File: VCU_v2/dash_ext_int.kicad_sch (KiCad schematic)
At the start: 55 parts, among them Q3 SP8K80TB1, Q4 SP8K80TB1, Q5 SP8K80TB1

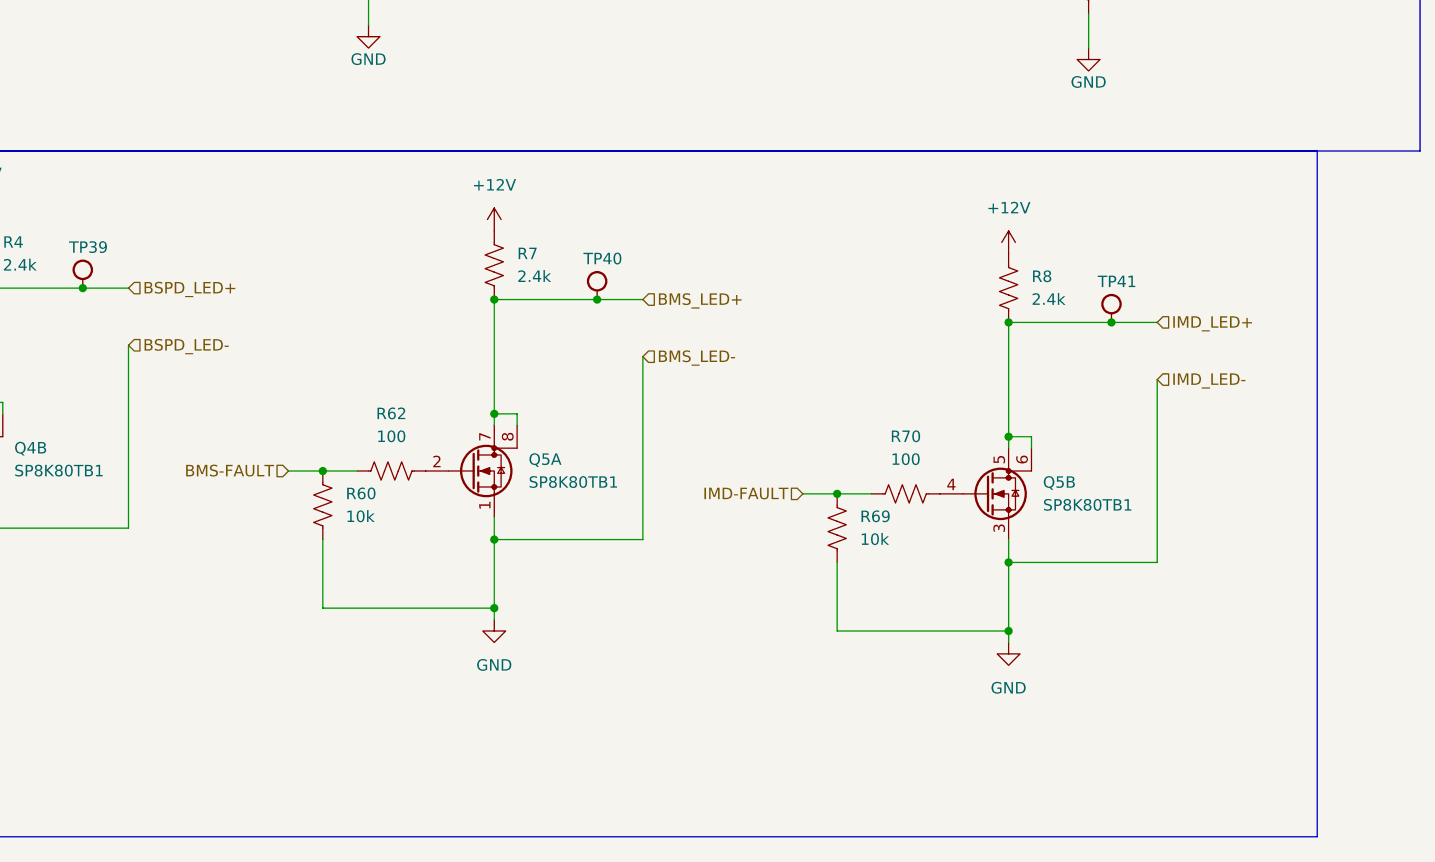
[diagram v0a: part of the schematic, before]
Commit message: reworked shutdown led logi c
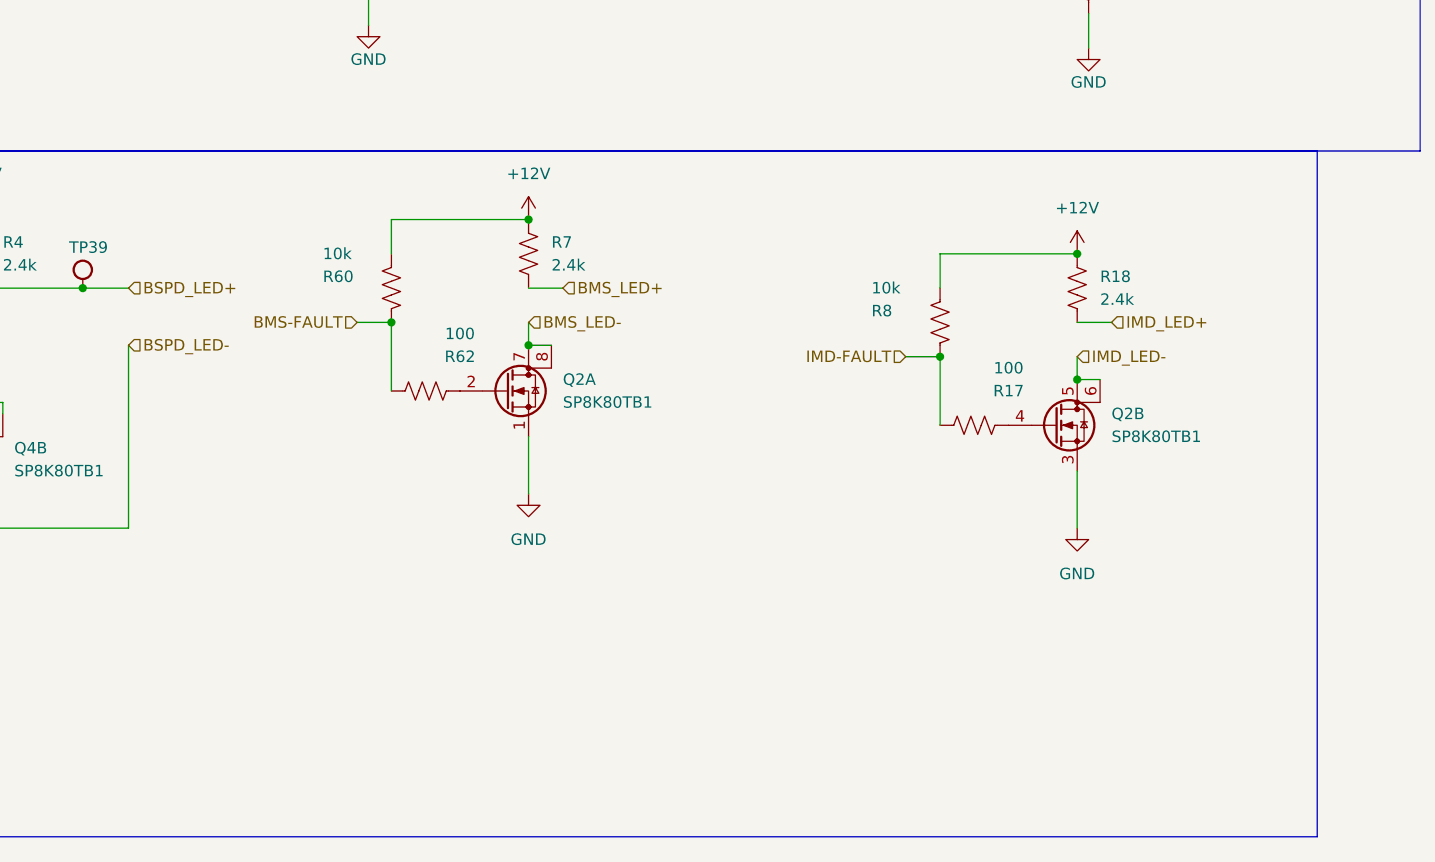
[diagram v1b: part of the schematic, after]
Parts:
- removed Q5: SP8K80TB1, Package_SO:SOP-8_3.76x4.96mm_P1.27mm, symbol Transistor_FET:Q_Dual_NMOS_S1G1S2G2D2D2D1D1
- removed R69: 10k, Resistor_SMD:R_0603_1608Metric_Pad0.98x0.95mm_HandSolder, symbol BFR Resistors:RMCF0603FT10K0
- removed R70: 100, Resistor_SMD:R_0603_1608Metric_Pad0.98x0.95mm_HandSolder, symbol BFR Resistors:RMCF0603FT100R
- removed R8: 2.4k, Resistor_SMD:R_0603_1608Metric_Pad0.98x0.95mm_HandSolder, symbol BFR Resistors:RMCF0603FT2K40
- removed TP40, TP41: RH-5015, TestPoint:TestPoint_Keystone_5015_Micro_Mini, symbol .Test-Point:RH-5015
- added Q2: SP8K80TB1, Package_SO:SOP-8_3.76x4.96mm_P1.27mm, symbol Transistor_FET:Q_Dual_NMOS_S1G1S2G2D2D2D1D1
- added R17: 100, Resistor_SMD:R_0603_1608Metric_Pad0.98x0.95mm_HandSolder, symbol BFR Resistors:RMCF0603FT100R
- added R18: 2.4k, Resistor_SMD:R_0603_1608Metric_Pad0.98x0.95mm_HandSolder, symbol BFR Resistors:RMCF0603FT2K40
- added R8: 10k, Resistor_SMD:R_0603_1608Metric_Pad0.98x0.95mm_HandSolder, symbol BFR Resistors:RMCF0603FT10K0
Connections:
- net +12V: now also R60.1, R18.2, R8.1
- net BMS-FAULT: now also R62.2; no longer R62.1
- net GND: now also Q2.1 (S), Q2.3 (S); no longer R60.1
- net IMD-FAULT: now also R17.2, R8.2
- net IMD_LED+: now also R18.1
- new net: Q2.4 (G), R17.1
- new net: Q2.2 (G), R62.1
- new net BMS_LED-: Q2.7 (D), Q2.8 (D)
- new net IMD_LED-: Q2.5 (D), Q2.6 (D)
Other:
- moved on the sheet: R60, R62, R7
